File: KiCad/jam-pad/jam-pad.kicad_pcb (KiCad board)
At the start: 2 copper layers, 131.4 x 57.1 mm, 82 parts, among them J1 USB_C, J2 PH_01x03_2.54mm, SW1 MX_Hotswap_LED_RGB, SW13 SW_Push, SW14 RotaryEncoder_Switch, SW15 SW_Push, SW2 MX_Hotswap_LED_RGB, SW3 MX_Hotswap_LED_RGB, SW4 MX_Hotswap_LED_RGB, SW5 MX_Hotswap_LED_RGB, SW6 MX_Hotswap_LED_RGB, SW7 MX_Hotswap_LED_RGB, SW8 MX_Hotswap_LED_RGB, SW9 MX_Hotswap_LED_RGB, U1 RP2040, U2 SN74LV1T34DBV, U3 W25Q16JVSNIQ, U4 MIC5319-3.3YD5, U5 SN74LV1T34DBV, Y1 ECS-120-18-33-JGN

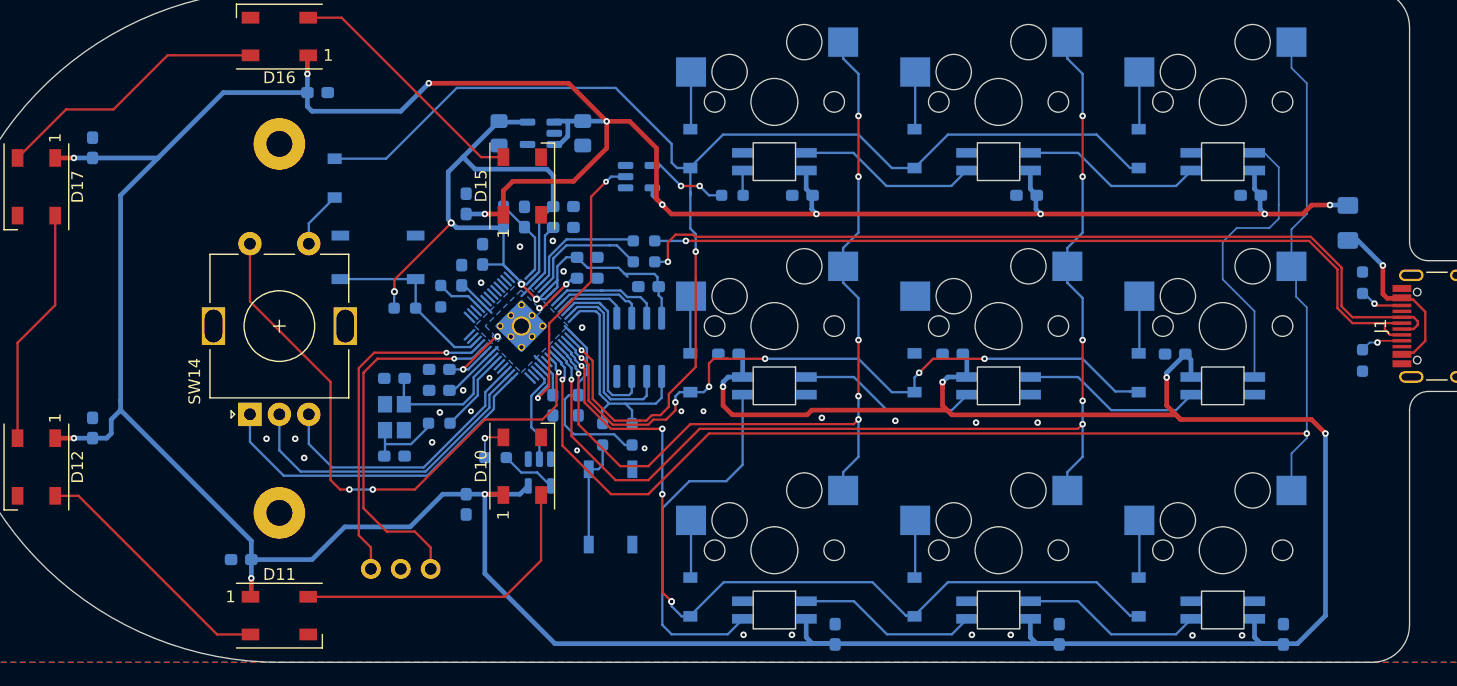
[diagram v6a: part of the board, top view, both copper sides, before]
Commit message: some more routing adjustments, move plate to its own folder. should be done besides footprint drc errors, deco, maybe replace rp2040 fp
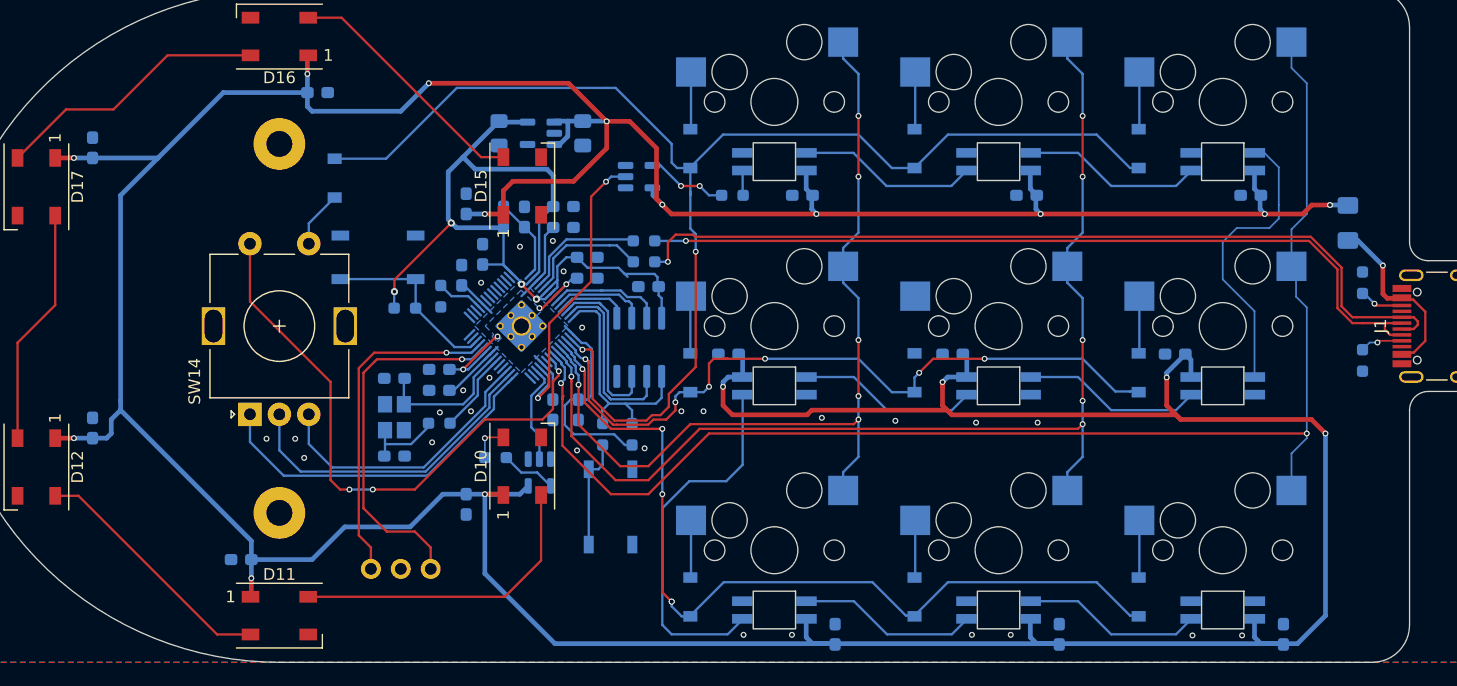
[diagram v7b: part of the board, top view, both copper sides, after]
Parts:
- moved C10 0.38 mm to (85.7, 61.1)
- moved C9 0.38 mm to (83.6, 61.1)
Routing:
- net +3V3: track 105.7 -> 106.6 mm
- net Row0: track 114.8 -> 115.4 mm

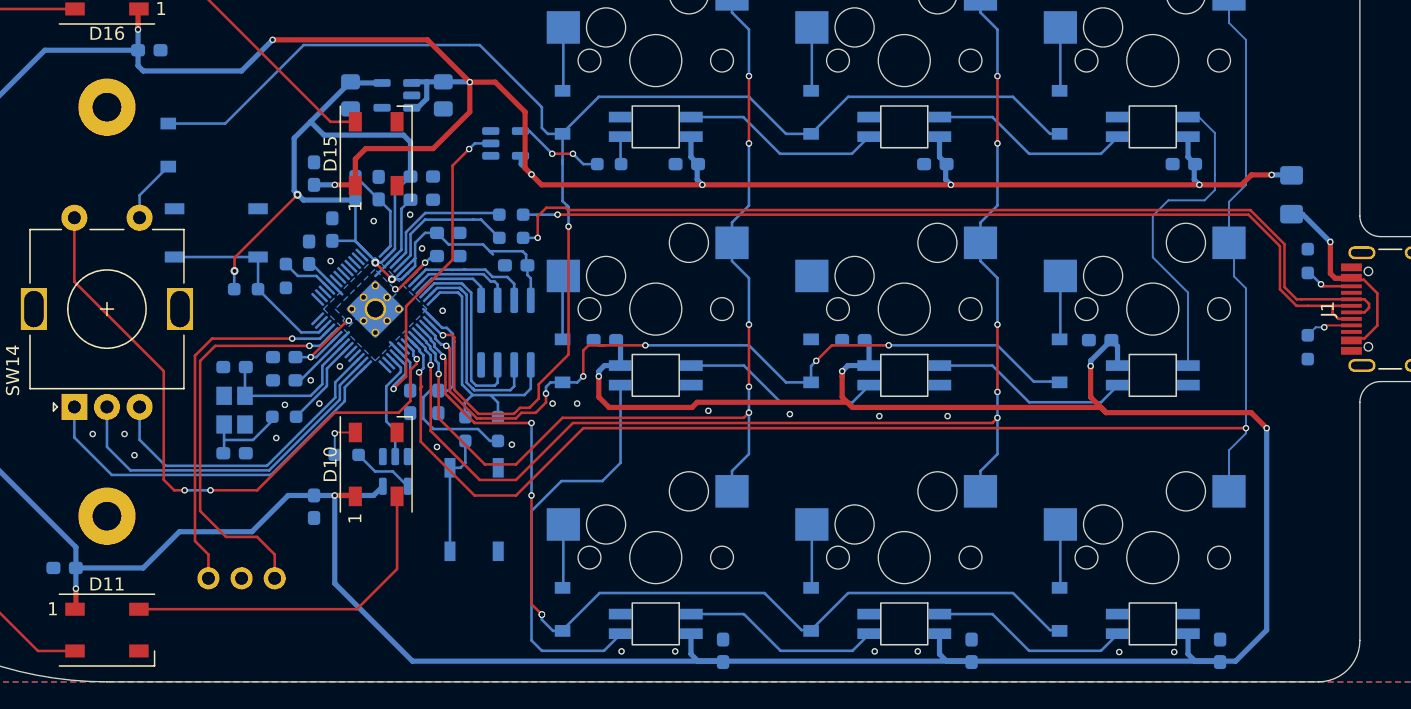
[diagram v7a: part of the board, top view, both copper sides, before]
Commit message: Remove unconnected tracks and pass schematic parity
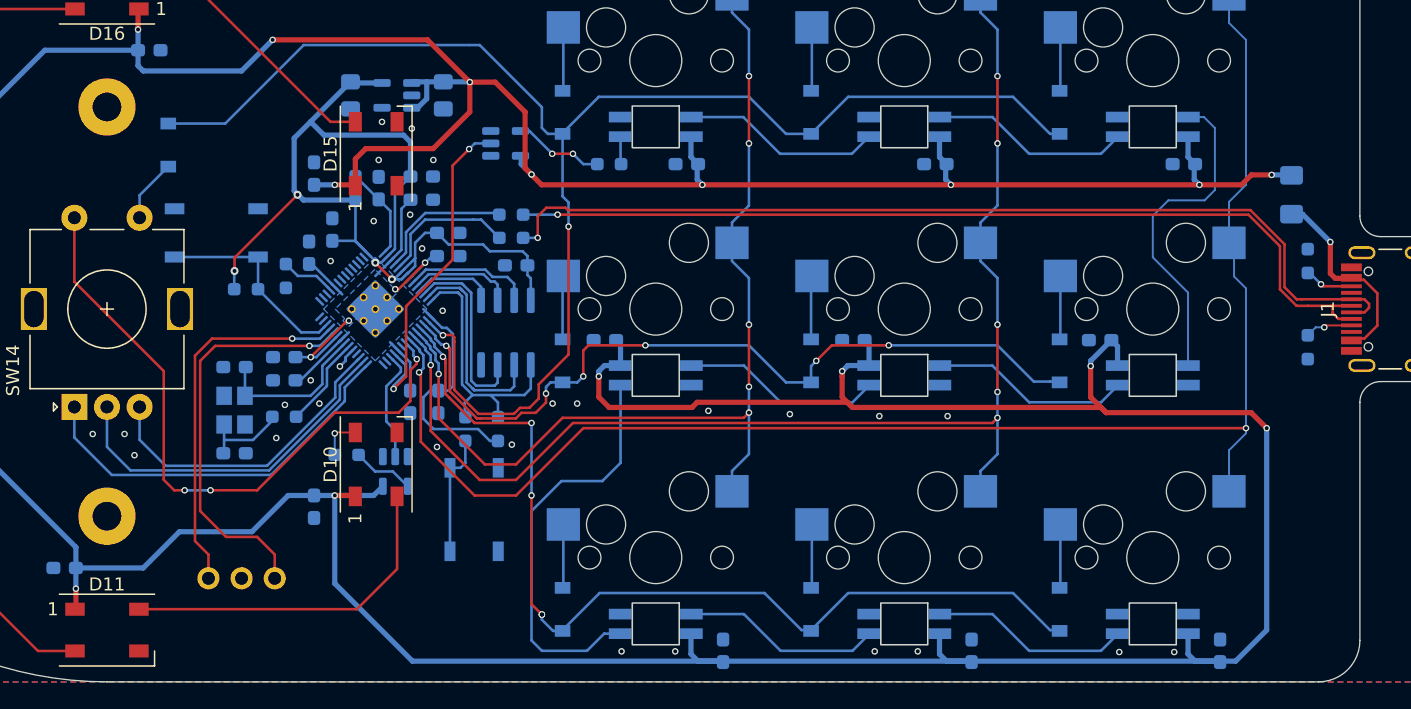
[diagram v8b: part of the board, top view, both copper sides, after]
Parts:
- removed REF** (x2): MountingHole_2.2mm_M2_Pad, MountingHole:MountingHole_2.2mm_M2_Pad
- added H1: MountingHole, MountingHole:MountingHole_2.2mm_M2_Pad, F.Cu at (60.3, 38.5)
- added H2: MountingHole, MountingHole:MountingHole_2.2mm_M2_Pad, F.Cu at (60.3, 69.8)
- U1: footprint jam-pad:RP2040-QFN-56_HandSoldering -> jam-pad:RP2040-QFN-56
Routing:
- net Net-(D5-A): track 0.00 -> 4.88 mm
- net GND: track 0.00 -> 1.67 mm, vias 27 -> 31
- net Col2: track 116.6 -> 115.7 mm
- net Net-(SW4B-DOUT): track 32.4 -> 31.9 mm
